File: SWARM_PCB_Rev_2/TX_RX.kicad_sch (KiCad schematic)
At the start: 84 parts

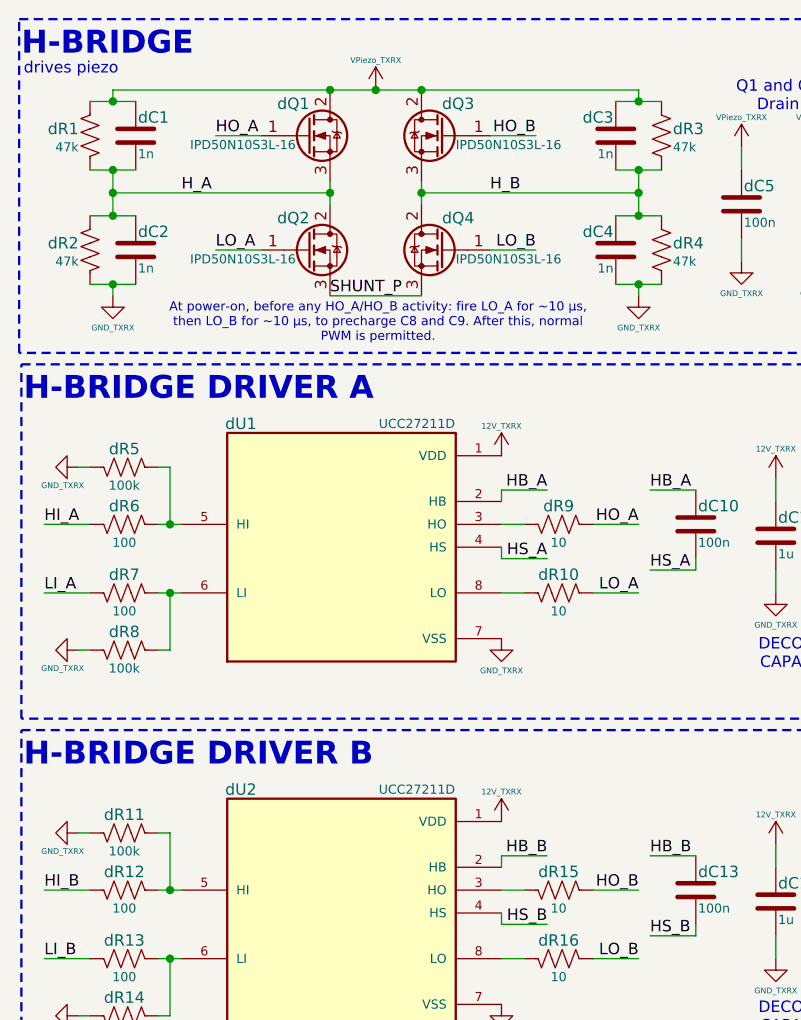
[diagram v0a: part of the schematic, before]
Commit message: Design review fixes: P7/P8/C10/C11/T4 + MPN audit
- P7: bR3 36k→4.3k, bR4 82k→4.3k (blue LEDs now 2.05mA each)
- P8: bD1 lib_id Diode:SS34→Device:D_TVS; embed D_TVS lib_symbol in POWER.kicad_sch
- C10: aR19 33Ω (RC0603FR-0733RL) added on SWO line (user-placed)
- C11: aFB1 footprint Resistor_SMD:R_0603_1608Metric→Inductor_SMD:L_0603_1608Metric
- T4: dD1/dD2 SS14-E3/61T bootstrap Schottky diodes added on HB_A/HB_B; MPN set
- BOM: MPNs added to J25–J28 (Samtec SSQ), aJ1/aJ4 (Harwin M50)
- DESIGN_REVIEW.md: close T4, T8/T9, P7, P8, C10, C11, H2, dC9, bL1/bL2 items

Co-Authored-By: Claude Sonnet 4.6 <noreply@anthropic.com>
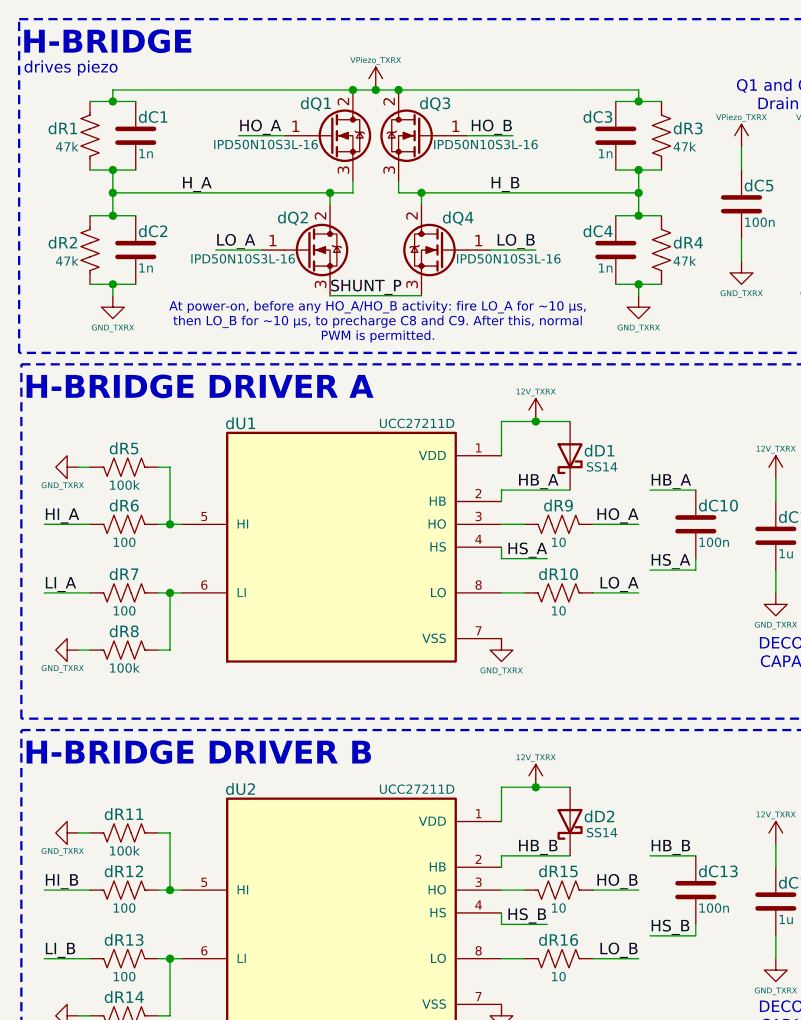
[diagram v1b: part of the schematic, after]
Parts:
- added dD1, dD2: SS14, Diode_SMD:D_SMA, symbol Diode:SS14
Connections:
- net 12V_TXRX: now also dD1.2 (A), dD2.2 (A)
- net HB_A: now also dD1.1 (K)
- net HB_B: now also dD2.1 (K)
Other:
- moved on the sheet: dQ1, dQ3
